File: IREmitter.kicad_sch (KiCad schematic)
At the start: 42 parts, among them J1 JST Connector, J2 JST Connector, J3 Right Header, J4 Left Header, SW1 Switch, U1 MOSFET, U2 H-Bridge, U3 Voltage Regulator, U4 STM32F205RGTx

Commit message: Reorganized schematics into a sheet hierarchy
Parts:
- removed A1: IR Receiver, ALS_PT19_315C_L177_TR8:XDCR_ALS-PT19-315C_L177_TR8, symbol Phototransistor_ALS-PT19-315C_L177_TR8:ALS-PT19-315C_L177_TR8
- removed C1, C4, C6: 4.7 µF, CL10A475KP8NNNC:CAPC1608X90N, symbol 4.7µFCapacitor_CL10A475KP8NNNC:CL10A475KP8NNNC
- removed C10, C9: 2.2 µF, CL10B225KP8NNNC:CAPC1608X90N, symbol 2.2µFCapacitor_CL10B225KP8NNNC:CL10B225KP8NNNC
- removed C11: 0.1 uF, 0.1µFCapacitor_footprints:CAP_0402_N_WAL-L, symbol 10uF_Capacitor_GRM188R61C106MAALD:GRM188R61C106MAALD
- removed C12, C13, C14, C16, C2, C5, C7, C8: 0.1 µF, 0.1µFCapacitor_footprints:CAP_0402_N_WAL-L, symbol 0.1µFCapacitor_2025-12-15_19-47-12:0402B104K160CT
- removed C15, C18, C3: 10 µF, CL21B106KOQNNNE:CAPC2012X140N, symbol 10µFCapacitor_CL21B106KOQNNNE:CL21B106KOQNNNE
- removed C17: 1 µF, CL10B105KP8NNNC:CAPC1608X90N, symbol 1µFCapacitor_CL10B105KP8NNNC:CL10B105KP8NNNC
- removed C19: 22 µF, CL21A226MPQNNNE:CAPC2012X140N, symbol 22µFCapacitor_CL21A226MPQNNNE:CL21A226MPQNNNE
- removed D1: IR Emitter, APT1608F3C:LED_APT1608F3C, symbol IRSensor_APT1608F3C:APT1608F3C
- removed D2: Power Indicator LED, WL-TMRC_5MM:WL-TMRC_5MM, symbol PowerIndicatorLED_WL-TMRC_5MM:WL-TMRC_5MM
- removed J1, J2: JST Connector, B2B_PH_K_S:JST_B2B-PH-K-S, symbol JSTConnector_B2B-PH-K-S:B2B-PH-K-S
- removed J3: Right Header, Connector_PinHeader_1.27mm:PinHeader_1x06_P1.27mm_Vertical_SMD_Pin1Right, symbol Connector:Conn_01x06_Pin
- removed J4: Left Header, Connector_PinHeader_1.27mm:PinHeader_1x06_P1.27mm_Vertical_SMD_Pin1Left, symbol Connector:Conn_01x06_Pin
- removed LED1, LED2: User LED, LED_LTL-4231N_LTO, symbol UserLED_2026-01-27_18-27-04:LTL-4231N
- removed R1: 51 Ohm, RC0805FR_0751RL:RESC2012X60N, symbol 51OhmResistor_RC0805FR-0751RL:RC0805FR-0751RL
- removed R2: 100 Ohm, CRCW0603100RFKEA:RESC1508X50N, symbol 100OhmResistor_CRCW0603100RFKEA:CRCW0603100RFKEA
- removed R3: 47 kOhm, RC0603FR_0747KL:RESC1608X55, symbol 47kOhmResistor_RC0603FR-0747KL:RC0603FR-0747KL
- removed R4: RMCF0805JT1K80, RMCF0805JT1K80:RESC2012X65N, symbol 1.8kOhm_RMCF0805JT1K80:RMCF0805JT1K80
- removed R5, R7: 10 kOhm, RMCF0805FT10K0:RESC2012X65N, symbol 10kOhmResistor_RMCF0805FT10K0:RMCF0805FT10K0
- removed R6: 35.2 Ohms, RN73R1JTTD35R2B25:RESC1608X55N, symbol 35.2ohmResistor_RN73R1JTTD35R2B25:RN73R1JTTD35R2B25
- removed R8, R9: 23.4 Ohms, RN73R1JTTD23R4B25:RESC1608X55N, symbol 23.4ohmResistor_RN73R1JTTD23R4B25:RN73R1JTTD23R4B25
- removed SW1: Switch, Switch_FSM4JSMATR_footprint:SW_4-1437565-2, symbol Switch_4-1437565-2:4-1437565-2
- removed U1: MOSFET, MOSFET_footprints:SOT-23_1_DIO, symbol MOSFET_2026-01-14_23-16-18:2N7002-7-F
- removed U2: H-Bridge, hbridge_L293DD:SOIC127P1032X265-20N, symbol HBridge_L293DD:L293DD
- removed U3: Voltage Regulator, AZ1117IH-3.3TRG1:SOT230P700X185-4N, symbol VoltageRegulator_AZ1117IH-3.3TRG1:AZ1117IH-3.3TRG1
- removed U4: STM32F205RGTx, Package_QFP:LQFP-64_10x10mm_P0.5mm, symbol MCU_ST_STM32F2:STM32F205RGTx
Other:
- added sheet MM-IR-Emitter (MM-IR-Emitter.kicad_sch)
- added sheet MM-IR-Receiver (MM-IR-Receiver.kicad_sch)
- added sheet MM-MCU (MM-MCU.kicad_sch)
- added sheet MM-Motor-Control (MM-Motor-Control.kicad_sch)
- added sheet MM-Power-Delivery (MM-Power-Delivery.kicad_sch)
- added sheet MM-Power-Indicator (MM-Power-Indicator.kicad_sch)
- added sheet MM-Reset-Button (MM-Reset-Button.kicad_sch)
- note removed: "IR Emitter"
- note removed: "IR Receiver"
- note removed: "Microcontroller"
- note removed: "Motor Control (H-Bridge)"
- note removed: "Power Delivery"
- note removed: "Power Indicator LED"
- note removed: "Reset Button"

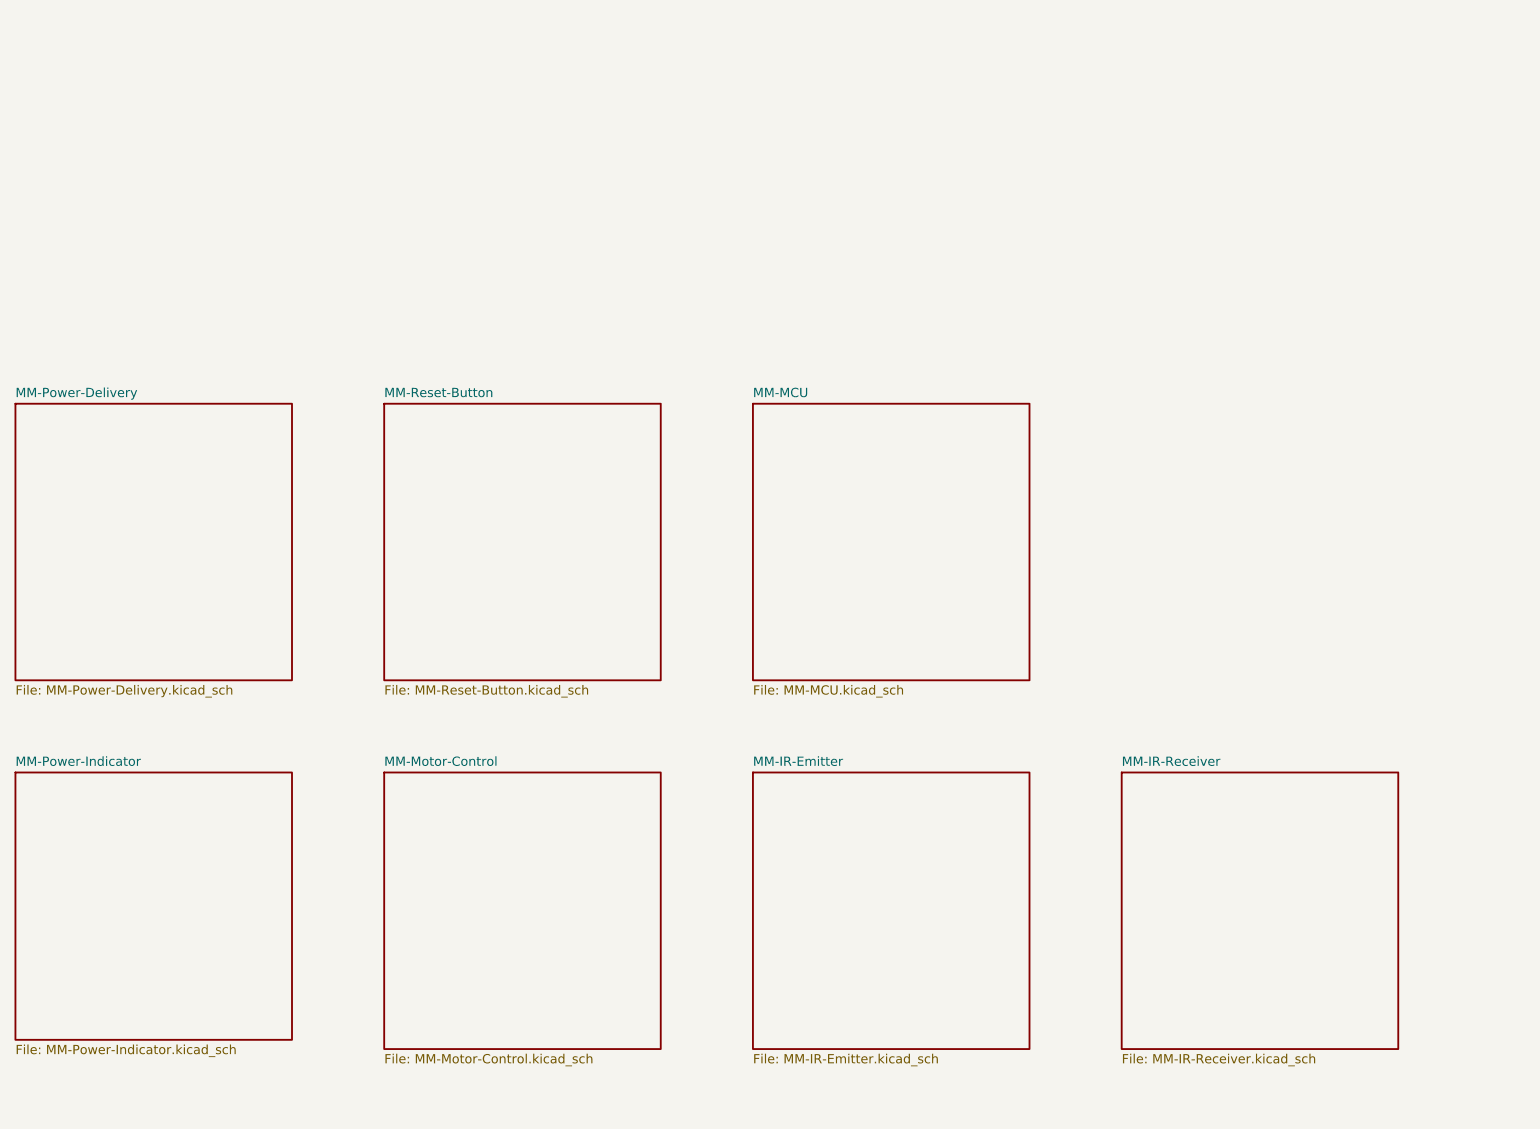
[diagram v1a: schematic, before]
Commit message: added power switch
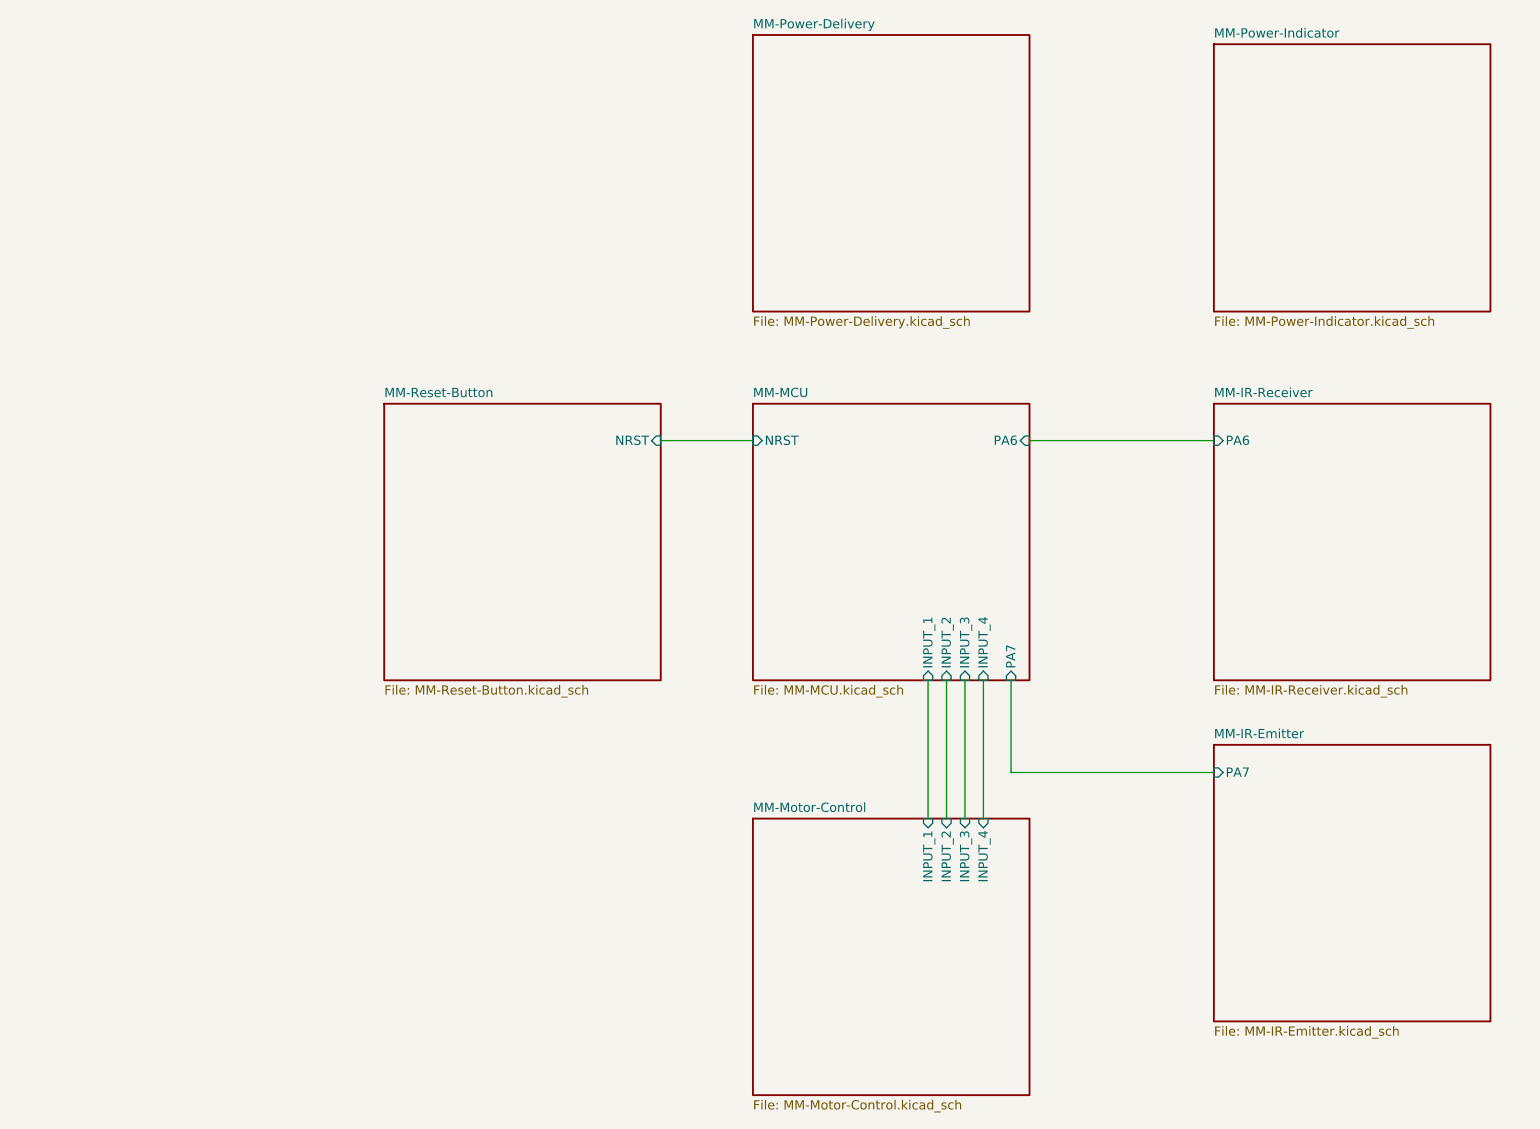
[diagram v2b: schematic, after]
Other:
- sheet MM-IR-Emitter ports: added PA7; removed none
- sheet MM-IR-Receiver ports: added PA6; removed none
- sheet MM-MCU ports: added INPUT_1, INPUT_2, INPUT_3, INPUT_4, NRST, PA6, PA7; removed none
- sheet MM-Motor-Control ports: added INPUT_1, INPUT_2, INPUT_3, INPUT_4; removed none
- sheet MM-Reset-Button ports: added  NRST; removed none
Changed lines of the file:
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@@
 	(generator_version "9.0")
 	(paper "A2")
+	(wire
+		(pts
+			(xy 266.7 93.98) (xy 292.1 93.98)
+		)
+		(stroke
+			(width 0)
+			(type default)
+		)
+	)
+	(wire
+		(pts
+			(xy 257.81 127) (xy 257.81 146.05)
+		)
+		(stroke
+			(width 0)
+			(type default)
+		)
+	)
+	(wire
+		(pts
+			(xy 260.35 127) (xy 260.35 146.05)
+		)
+		(stroke
+			(width 0)
+			(type default)
+		)
+	)
+	(wire
+		(pts
+			(xy 255.27 127) (xy 255.27 146.05)
+		)
+		(stroke
+			(width 0)
+			(type default)
+		)
+	)
+	(wire
+		(pts
+			(xy 215.9 93.98) (xy 228.6 93.98)
+		)
+		(stroke
+			(width 0)
+			(type default)
+		)
+	)
+	(wire
+		(pts
+			(xy 264.16 139.7) (xy 292.1 139.7)
+		)
+		(stroke
+			(width 0)
+			(type default)
+		)
+	)
+	(wire
+		(pts
+			(xy 252.73 127) (xy 252.73 146.05)
+		)
+		(stroke
+			(width 0)
+			(type default)
+		)
+	)
+	(wire
+		(pts
+			(xy 264.16 127) (xy 264.16 139.7)
+		)
+		(stroke
+			(width 0)
+			(type default)
+		)
+	)
 	(sheet
 		(at 177.8 88.9)
@@
 			)
 		)
+		(pin " NRST" input
+			(at 215.9 93.98 0)
+			(effects
+				(font
+					(size 1.27 1.27)
+				)
+				(justify right)
+			)
+		)
 		(instances
 			(project "IREmitter"
@@
 	)
 	(sheet
-		(at 127 88.9)
+		(at 228.6 38.1)
 		(size 38.1 38.1)
 		(exclude_from_sim no)
@@
 		)
 		(property "Sheetname" "MM-Power-Delivery"
-			(at 127 88.1376 0)
+			(at 228.6 37.3376 0)
 			(effects
 				(font
@@
 		)
 		(property "Sheetfile" "MM-Power-Delivery.kicad_sch"
-			(at 127 127.6354 0)
+			(at 228.6 76.8354 0)
 			(effects
 				(font
@@
 	)
 	(sheet
-		(at 177.8 139.7)
+		(at 228.6 146.05)
 		(size 38.1 38.1)
 		(exclude_from_sim no)
@@
 		)
 		(property "Sheetname" "MM-Motor-Control"
-			(at 177.8 138.9376 0)
+			(at 228.6 145.2876 0)
 			(effects
 				(font
@@
 		)
 		(property "Sheetfile" "MM-Motor-Control.kicad_sch"
-			(at 177.8 178.4354 0)
-			(effects
-				(font
-					(size 1.27 1.27)
-				)
-				(justify left top)
+			(at 228.6 184.7854 0)
+			(effects
+				(font
+					(size 1.27 1.27)
+				)
+				(justify left top)
+			)
+		)
+		(pin "INPUT_3" input
+			(at 257.81 146.05 90)
+			(effects
+				(font
+					(size 1.27 1.27)
+				)
+				(justify right)
+			)
+		)
+		(pin "INPUT_2" input
+			(at 255.27 146.05 90)
+			(effects
+				(font
+					(size 1.27 1.27)
+				)
+				(justify right)
+			)
+		)
+		(pin "INPUT_4" input
+			(at 260.35 146.05 90)
+			(effects
+				(font
+					(size 1.27 1.27)
+				)
+				(justify right)
+			)
+		)
+		(pin "INPUT_1" input
+			(at 252.73 146.05 90)
+			(effects
+				(font
+					(size 1.27 1.27)
+				)
+				(justify right)
 			)
 		)
@@
 			)
 		)
+		(pin "NRST" input
+			(at 228.6 93.98 180)
+			(effects
+				(font
+					(size 1.27 1.27)
+				)
+				(justify left)
+			)
+		)
+		(pin "PA6" input
+			(at 266.7 93.98 0)
+			(effects
+				(font
+					(size 1.27 1.27)
+				)
+				(justify right)
+			)
+		)
+		(pin "INPUT_4" input
+			(at 260.35 127 270)
+			(effects
+				(font
+					(size 1.27 1.27)
+				)
+				(justify left)
+			)
+		)
+		(pin "PA7" input
+			(at 264.16 127 270)
+			(effects
+				(font
+					(size 1.27 1.27)
+				)
+				(justify left)
+			)
+		)
+		(pin "INPUT_1" input
+			(at 252.73 127 270)
+			(effects
+				(font
+					(size 1.27 1.27)
+				)
+				(justify left)
+			)
+		)
+		(pin "INPUT_3" input
+			(at 257.81 127 270)
+			(effects
+				(font
+					(size 1.27 1.27)
+				)
+				(justify left)
+			)
+		)
+		(pin "INPUT_2" input
+			(at 255.27 127 270)
+			(effects
+				(font
+					(size 1.27 1.27)
+				)
+				(justify left)
+			)
+		)
 		(instances
 			(project "IREmitter"
@@
 	)
 	(sheet
-		(at 127 139.7)
+		(at 292.1 39.37)
 		(size 38.1 36.83)
 		(exclude_from_sim no)
@@
 		)
 		(property "Sheetname" "MM-Power-Indicator"
-			(at 127 138.9376 0)
+			(at 292.1 38.6076 0)
 			(effects
 				(font
@@
 		)
 		(property "Sheetfile" "MM-Power-Indicator.kicad_sch"
-			(at 127 177.1654 0)
+			(at 292.1 76.8354 0)
 			(effects
 				(font
@@
 	)
 	(sheet
-		(at 279.4 139.7)
+		(at 292.1 88.9)
 		(size 38.1 38.1)
 		(exclude_from_sim no)
@@
 		)
 		(property "Sheetname" "MM-IR-Receiver"
-			(at 279.4 138.9376 0)
+			(at 292.1 88.1376 0)
 			(effects
 				(font
@@
 		)
 		(property "Sheetfile" "MM-IR-Receiver.kicad_sch"
-			(at 279.4 178.4354 0)
-			(effects
-				(font
-					(size 1.27 1.27)
-				)
-				(justify left top)
+			(at 292.1 127.6354 0)
+			(effects
+				(font
+					(size 1.27 1.27)
+				)
+				(justify left top)
+			)
+		)
+		(pin "PA6" input
+			(at 292.1 93.98 180)
+			(effects
+				(font
+					(size 1.27 1.27)
+				)
+				(justify left)
 			)
 		)
@@
 	)
 	(sheet
-		(at 228.6 139.7)
+		(at 292.1 135.89)
 		(size 38.1 38.1)
 		(exclude_from_sim no)
@@
 		)
 		(property "Sheetname" "MM-IR-Emitter"
-			(at 228.6 138.9376 0)
+			(at 292.1 135.1276 0)
 			(effects
 				(font
@@
 		)
 		(property "Sheetfile" "MM-IR-Emitter.kicad_sch"
-			(at 228.6 178.4354 0)
-			(effects
-				(font
-					(size 1.27 1.27)
-				)
-				(justify left top)
-			)
-		)
+			(at 292.1 174.6254 0)
+			(effects
+				(font
+					(size 1.27 1.27)
+				)
+				(justify left top)
+			)
+		)
+		(pin "PA7" input
+			(at 292.1 139.7 180)
+			(effects
+				(font
+					(size 1.27 1.27)
+				)
+				(justify left)
+			)
+		)
